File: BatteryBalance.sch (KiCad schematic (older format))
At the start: 49 parts, among them J8 Conn_02x07_Counter_Clockwise, Q10 FQD5N20L, Q11 FQD5N20L, Q12 FQD5N20L, Q13 FQD5N20L, Q14 FQD5N20L, Q15 FQD5N20L, Q4 FQD5N20L, Q5 FQD5N20L, Q6 FQD5N20L, Q7 FQD5N20L, Q8 FQD5N20L, Q9 FQD5N20L

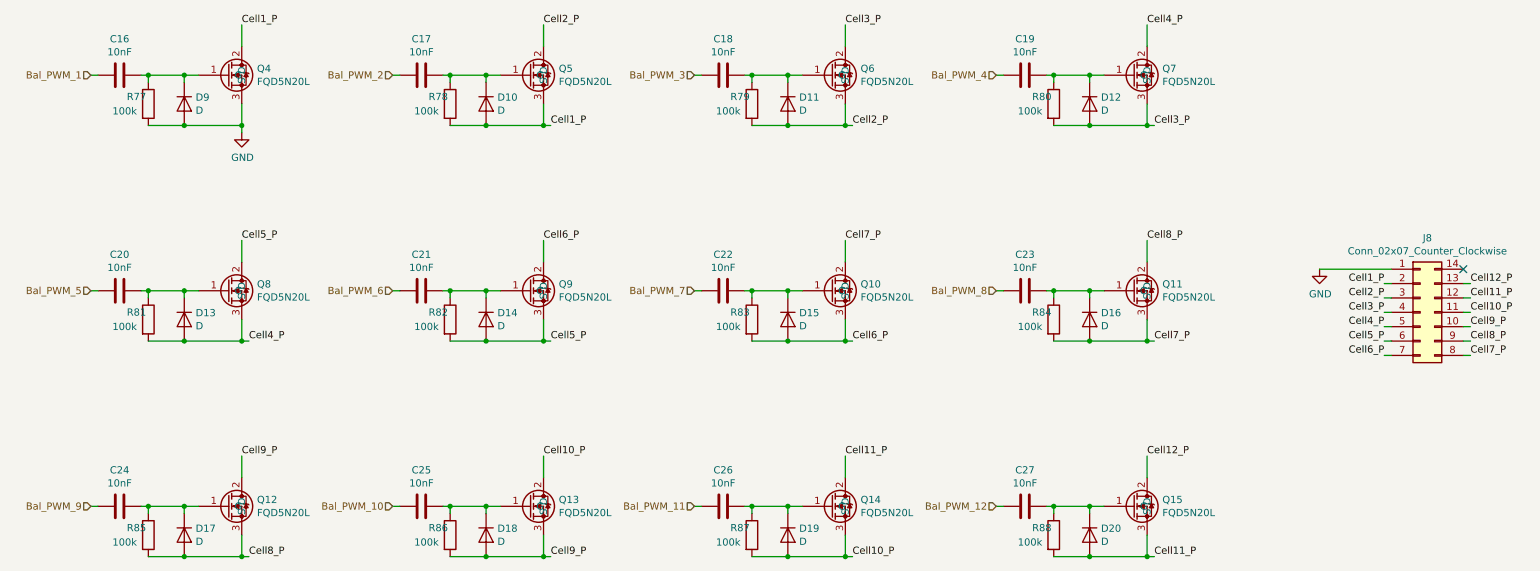
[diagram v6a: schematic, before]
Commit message: Added JST power connect and fixed some footprints
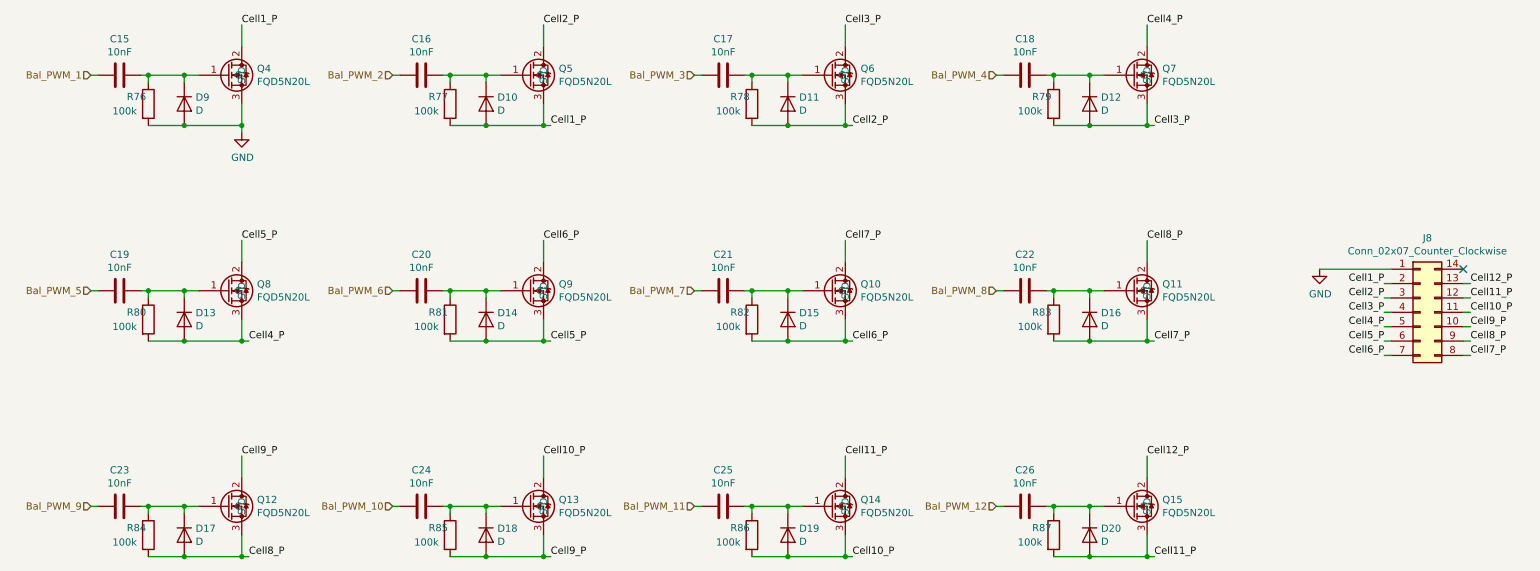
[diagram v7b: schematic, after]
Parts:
- renumbered C16 to C15, C17 to C16, C18 to C17, C19 to C18, C20 to C19, C21 to C20, C22 to C21, C23 to C22, C24 to C23, C25 to C24, C26 to C25, C27 to C26, R77 to R76, R78 to R77, R79 to R78, R80 to R79, R81 to R80, R82 to R81, R83 to R82, R84 to R83, R85 to R84, R86 to R85, R87 to R86, R88 to R87
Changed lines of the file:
@@
 P 9650 2850
 AR Path="/5F70A721/5F78CA1C" Ref="#PWR?"  Part="1"
-AR Path="/5F7870B7/5F78CA1C" Ref="#PWR089"  Part="1"
-F 0 "#PWR089" H 9650 2600 50  0001 C CNN
+AR Path="/5F7870B7/5F78CA1C" Ref="#PWR087"  Part="1"
+F 0 "#PWR087" H 9650 2600 50  0001 C CNN
 F 1 "GND" H 9655 2677 50  0000 C CNN
 F 2 "" H 9650 2850 50  0001 C CNN
@@
 NoConn ~ 10650 2850
 $Comp
-L Device:C C16
+L Device:C C15
 U 1 1 5F78D337
 P 1300 1500
-F 0 "C16" V 1048 1500 50  0000 C CNN
+F 0 "C15" V 1048 1500 50  0000 C CNN
 F 1 "10nF" V 1139 1500 50  0000 C CNN
 F 2 "Capacitor_SMD:C_1206_3216Metric" H 1338 1350 50  0001 C CNN
@@
 $EndComp
 $Comp
-L Device:R R77
+L Device:R R76
 U 1 1 5F79167A
 P 1500 1700
-F 0 "R77" H 1350 1750 50  0000 L CNN
+F 0 "R76" H 1350 1750 50  0000 L CNN
 F 1 "100k" H 1250 1650 50  0000 L CNN
 F 2 "Resistor_SMD:R_0603_1608Metric_Pad1.05x0.95mm_HandSolder" V 1430 1700 50  0001 C CNN
@@
 P 2150 1900
 AR Path="/5F70A721/5F793673" Ref="#PWR?"  Part="1"
-AR Path="/5F7870B7/5F793673" Ref="#PWR088"  Part="1"
-F 0 "#PWR088" H 2150 1650 50  0001 C CNN
+AR Path="/5F7870B7/5F793673" Ref="#PWR086"  Part="1"
+F 0 "#PWR086" H 2150 1650 50  0001 C CNN
 F 1 "GND" H 2155 1727 50  0000 C CNN
 F 2 "" H 2150 1900 50  0001 C CNN
@@
 Connection ~ 2150 1850
 $Comp
-L Device:C C17
+L Device:C C16
 U 1 1 5F796EE6
 P 3400 1500
-F 0 "C17" V 3148 1500 50  0000 C CNN
+F 0 "C16" V 3148 1500 50  0000 C CNN
 F 1 "10nF" V 3239 1500 50  0000 C CNN
 F 2 "Capacitor_SMD:C_1206_3216Metric" H 3438 1350 50  0001 C CNN
@@
 $EndComp
 $Comp
-L Device:R R78
+L Device:R R77
 U 1 1 5F796EF2
 P 3600 1700
-F 0 "R78" H 3450 1750 50  0000 L CNN
+F 0 "R77" H 3450 1750 50  0000 L CNN
 F 1 "100k" H 3350 1650 50  0000 L CNN
 F 2 "Resistor_SMD:R_0603_1608Metric_Pad1.05x0.95mm_HandSolder" V 3530 1700 50  0001 C CNN
@@
 	4250 1300 4250 1150
 $Comp
-L Device:C C18
+L Device:C C17
 U 1 1 5F79E64F
 P 5500 1500
-F 0 "C18" V 5248 1500 50  0000 C CNN
+F 0 "C17" V 5248 1500 50  0000 C CNN
 F 1 "10nF" V 5339 1500 50  0000 C CNN
 F 2 "Capacitor_SMD:C_1206_3216Metric" H 5538 1350 50  0001 C CNN
@@
 $EndComp
 $Comp
-L Device:R R79
+L Device:R R78
 U 1 1 5F79E65B
 P 5700 1700
-F 0 "R79" H 5550 1750 50  0000 L CNN
+F 0 "R78" H 5550 1750 50  0000 L CNN
 F 1 "100k" H 5450 1650 50  0000 L CNN
 F 2 "Resistor_SMD:R_0603_1608Metric_Pad1.05x0.95mm_HandSolder" V 5630 1700 50  0001 C CNN
@@
 	6350 1300 6350 1150
 $Comp
-L Device:C C19
+L Device:C C18
 U 1 1 5F7A2D2F
 P 7600 1500
-F 0 "C19" V 7348 1500 50  0000 C CNN
+F 0 "C18" V 7348 1500 50  0000 C CNN
 F 1 "10nF" V 7439 1500 50  0000 C CNN
 F 2 "Capacitor_SMD:C_1206_3216Metric" H 7638 1350 50  0001 C CNN
@@
 $EndComp
 $Comp
-L Device:R R80
+L Device:R R79
 U 1 1 5F7A2D3B
 P 7800 1700
-F 0 "R80" H 7650 1750 50  0000 L CNN
+F 0 "R79" H 7650 1750 50  0000 L CNN
 F 1 "100k" H 7550 1650 50  0000 L CNN
 F 2 "Resistor_SMD:R_0603_1608Metric_Pad1.05x0.95mm_HandSolder" V 7730 1700 50  0001 C CNN
@@
 	8450 1300 8450 1150
 $Comp
-L Device:C C20
+L Device:C C19
 U 1 1 5F7ADC89
 P 1300 3000
-F 0 "C20" V 1048 3000 50  0000 C CNN
+F 0 "C19" V 1048 3000 50  0000 C CNN
 F 1 "10nF" V 1139 3000 50  0000 C CNN
 F 2 "Capacitor_SMD:C_1206_3216Metric" H 1338 2850 50  0001 C CNN
@@
 $EndComp
 $Comp
-L Device:R R81
+L Device:R R80
 U 1 1 5F7ADC95
 P 1500 3200
-F 0 "R81" H 1350 3250 50  0000 L CNN
+F 0 "R80" H 1350 3250 50  0000 L CNN
 F 1 "100k" H 1250 3150 50  0000 L CNN
 F 2 "Resistor_SMD:R_0603_1608Metric_Pad1.05x0.95mm_HandSolder" V 1430 3200 50  0001 C CNN
@@
 	2150 2800 2150 2650
 $Comp
-L Device:C C21
+L Device:C C20
 U 1 1 5F7ADCB6
 P 3400 3000
-F 0 "C21" V 3148 3000 50  0000 C CNN
+F 0 "C20" V 3148 3000 50  0000 C CNN
 F 1 "10nF" V 3239 3000 50  0000 C CNN
 F 2 "Capacitor_SMD:C_1206_3216Metric" H 3438 2850 50  0001 C CNN
@@
 $EndComp
 $Comp
-L Device:R R82
+L Device:R R81
 U 1 1 5F7ADCC2
 P 3600 3200
-F 0 "R82" H 3450 3250 50  0000 L CNN
+F 0 "R81" H 3450 3250 50  0000 L CNN
 F 1 "100k" H 3350 3150 50  0000 L CNN
 F 2 "Resistor_SMD:R_0603_1608Metric_Pad1.05x0.95mm_HandSolder" V 3530 3200 50  0001 C CNN
@@
 	4250 2800 4250 2650
 $Comp
-L Device:C C22
+L Device:C C21
 U 1 1 5F7ADCE3
 P 5500 3000
-F 0 "C22" V 5248 3000 50  0000 C CNN
+F 0 "C21" V 5248 3000 50  0000 C CNN
 F 1 "10nF" V 5339 3000 50  0000 C CNN
 F 2 "Capacitor_SMD:C_1206_3216Metric" H 5538 2850 50  0001 C CNN
@@
 $EndComp
 $Comp
-L Device:R R83
+L Device:R R82
 U 1 1 5F7ADCEF
 P 5700 3200
-F 0 "R83" H 5550 3250 50  0000 L CNN
+F 0 "R82" H 5550 3250 50  0000 L CNN
 F 1 "100k" H 5450 3150 50  0000 L CNN
 F 2 "Resistor_SMD:R_0603_1608Metric_Pad1.05x0.95mm_HandSolder" V 5630 3200 50  0001 C CNN
@@
 	6350 2800 6350 2650
 $Comp
-L Device:C C23
+L Device:C C22
 U 1 1 5F7ADD10
 P 7600 3000
-F 0 "C23" V 7348 3000 50  0000 C CNN
+F 0 "C22" V 7348 3000 50  0000 C CNN
 F 1 "10nF" V 7439 3000 50  0000 C CNN
 F 2 "Capacitor_SMD:C_1206_3216Metric" H 7638 2850 50  0001 C CNN
@@
 $EndComp
 $Comp
-L Device:R R84
+L Device:R R83
 U 1 1 5F7ADD1C
 P 7800 3200
-F 0 "R84" H 7650 3250 50  0000 L CNN
+F 0 "R83" H 7650 3250 50  0000 L CNN
 F 1 "100k" H 7550 3150 50  0000 L CNN
 F 2 "Resistor_SMD:R_0603_1608Metric_Pad1.05x0.95mm_HandSolder" V 7730 3200 50  0001 C CNN
@@
 	8450 2800 8450 2650
 $Comp
-L Device:C C24
+L Device:C C23
 U 1 1 5F7BAE22
 P 1300 4500
-F 0 "C24" V 1048 4500 50  0000 C CNN
+F 0 "C23" V 1048 4500 50  0000 C CNN
 F 1 "10nF" V 1139 4500 50  0000 C CNN
 F 2 "Capacitor_SMD:C_1206_3216Metric" H 1338 4350 50  0001 C CNN
@@
 $EndComp
 $Comp
-L Device:R R85
+L Device:R R84
 U 1 1 5F7BAE2E
 P 1500 4700
-F 0 "R85" H 1350 4750 50  0000 L CNN
+F 0 "R84" H 1350 4750 50  0000 L CNN
 F 1 "100k" H 1250 4650 50  0000 L CNN
 F 2 "Resistor_SMD:R_0603_1608Metric_Pad1.05x0.95mm_HandSolder" V 1430 4700 50  0001 C CNN
@@
 	2150 4300 2150 4150
 $Comp
-L Device:C C25
+L Device:C C24
 U 1 1 5F7BAE4F
 P 3400 4500
-F 0 "C25" V 3148 4500 50  0000 C CNN
+F 0 "C24" V 3148 4500 50  0000 C CNN
 F 1 "10nF" V 3239 4500 50  0000 C CNN
 F 2 "Capacitor_SMD:C_1206_3216Metric" H 3438 4350 50  0001 C CNN
@@
 $EndComp
 $Comp
-L Device:R R86
+L Device:R R85
 U 1 1 5F7BAE5B
 P 3600 4700
-F 0 "R86" H 3450 4750 50  0000 L CNN
+F 0 "R85" H 3450 4750 50  0000 L CNN
 F 1 "100k" H 3350 4650 50  0000 L CNN
 F 2 "Resistor_SMD:R_0603_1608Metric_Pad1.05x0.95mm_HandSolder" V 3530 4700 50  0001 C CNN
@@
 	4250 4300 4250 4150
 $Comp
-L Device:C C26
+L Device:C C25
 U 1 1 5F7BAE7C
 P 5500 4500
-F 0 "C26" V 5248 4500 50  0000 C CNN
+F 0 "C25" V 5248 4500 50  0000 C CNN
 F 1 "10nF" V 5339 4500 50  0000 C CNN
 F 2 "Capacitor_SMD:C_1206_3216Metric" H 5538 4350 50  0001 C CNN
@@
 $EndComp
 $Comp
-L Device:R R87
+L Device:R R86
 U 1 1 5F7BAE88
 P 5700 4700
-F 0 "R87" H 5550 4750 50  0000 L CNN
+F 0 "R86" H 5550 4750 50  0000 L CNN
 F 1 "100k" H 5450 4650 50  0000 L CNN
 F 2 "Resistor_SMD:R_0603_1608Metric_Pad1.05x0.95mm_HandSolder" V 5630 4700 50  0001 C CNN
@@
 	6350 4300 6350 4150
 $Comp
-L Device:C C27
+L Device:C C26
 U 1 1 5F7BAEA9
 P 7600 4500
-F 0 "C27" V 7348 4500 50  0000 C CNN
+F 0 "C26" V 7348 4500 50  0000 C CNN
 F 1 "10nF" V 7439 4500 50  0000 C CNN
 F 2 "Capacitor_SMD:C_1206_3216Metric" H 7638 4350 50  0001 C CNN
@@
 $EndComp
 $Comp
-L Device:R R88
+L Device:R R87
 U 1 1 5F7BAEB5
 P 7800 4700
-F 0 "R88" H 7650 4750 50  0000 L CNN
+F 0 "R87" H 7650 4750 50  0000 L CNN
 F 1 "100k" H 7550 4650 50  0000 L CNN
 F 2 "Resistor_SMD:R_0603_1608Metric_Pad1.05x0.95mm_HandSolder" V 7730 4700 50  0001 C CNN

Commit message: Refactored some naming
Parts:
- renumbered J8 to J7
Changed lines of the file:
@@
 P 9650 2850
 AR Path="/5F70A721/5F78CA1C" Ref="#PWR?"  Part="1"
-AR Path="/5F7870B7/5F78CA1C" Ref="#PWR087"  Part="1"
-F 0 "#PWR087" H 9650 2600 50  0001 C CNN
+AR Path="/5F7870B7/5F78CA1C" Ref="#PWR086"  Part="1"
+F 0 "#PWR086" H 9650 2600 50  0001 C CNN
 F 1 "GND" H 9655 2677 50  0000 C CNN
 F 2 "" H 9650 2850 50  0001 C CNN
@@
 Cell6_P
 $Comp
-L Connector_Generic:Conn_02x07_Counter_Clockwise J8
+L Connector_Generic:Conn_02x07_Counter_Clockwise J7
 U 1 1 5F78CA28
 P 10350 3150
-F 0 "J8" H 10400 3667 50  0000 C CNN
+F 0 "J7" H 10400 3667 50  0000 C CNN
 F 1 "Conn_02x07_Counter_Clockwise" H 10400 3576 50  0000 C CNN
 F 2 "Connector_PinHeader_2.54mm:PinHeader_2x07_P2.54mm_Vertical" H 10350 3150 50  0001 C CNN
@@
 P 2150 1900
 AR Path="/5F70A721/5F793673" Ref="#PWR?"  Part="1"
-AR Path="/5F7870B7/5F793673" Ref="#PWR086"  Part="1"
-F 0 "#PWR086" H 2150 1650 50  0001 C CNN
+AR Path="/5F7870B7/5F793673" Ref="#PWR085"  Part="1"
+F 0 "#PWR085" H 2150 1650 50  0001 C CNN
 F 1 "GND" H 2155 1727 50  0000 C CNN
 F 2 "" H 2150 1900 50  0001 C CNN
